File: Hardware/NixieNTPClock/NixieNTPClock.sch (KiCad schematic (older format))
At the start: 54 parts, among them J1 Conn_01x02_Male, Q1 BC850, Q2 Q_NMOS_GDS, Q3 FQT4N25TF, Q4 FQT4N25TF, Q5 FQT4N25TF, Q6 FQT4N25TF, U1 74HC7014, U10 DS18B20, U11 ESP32-nodeMCU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

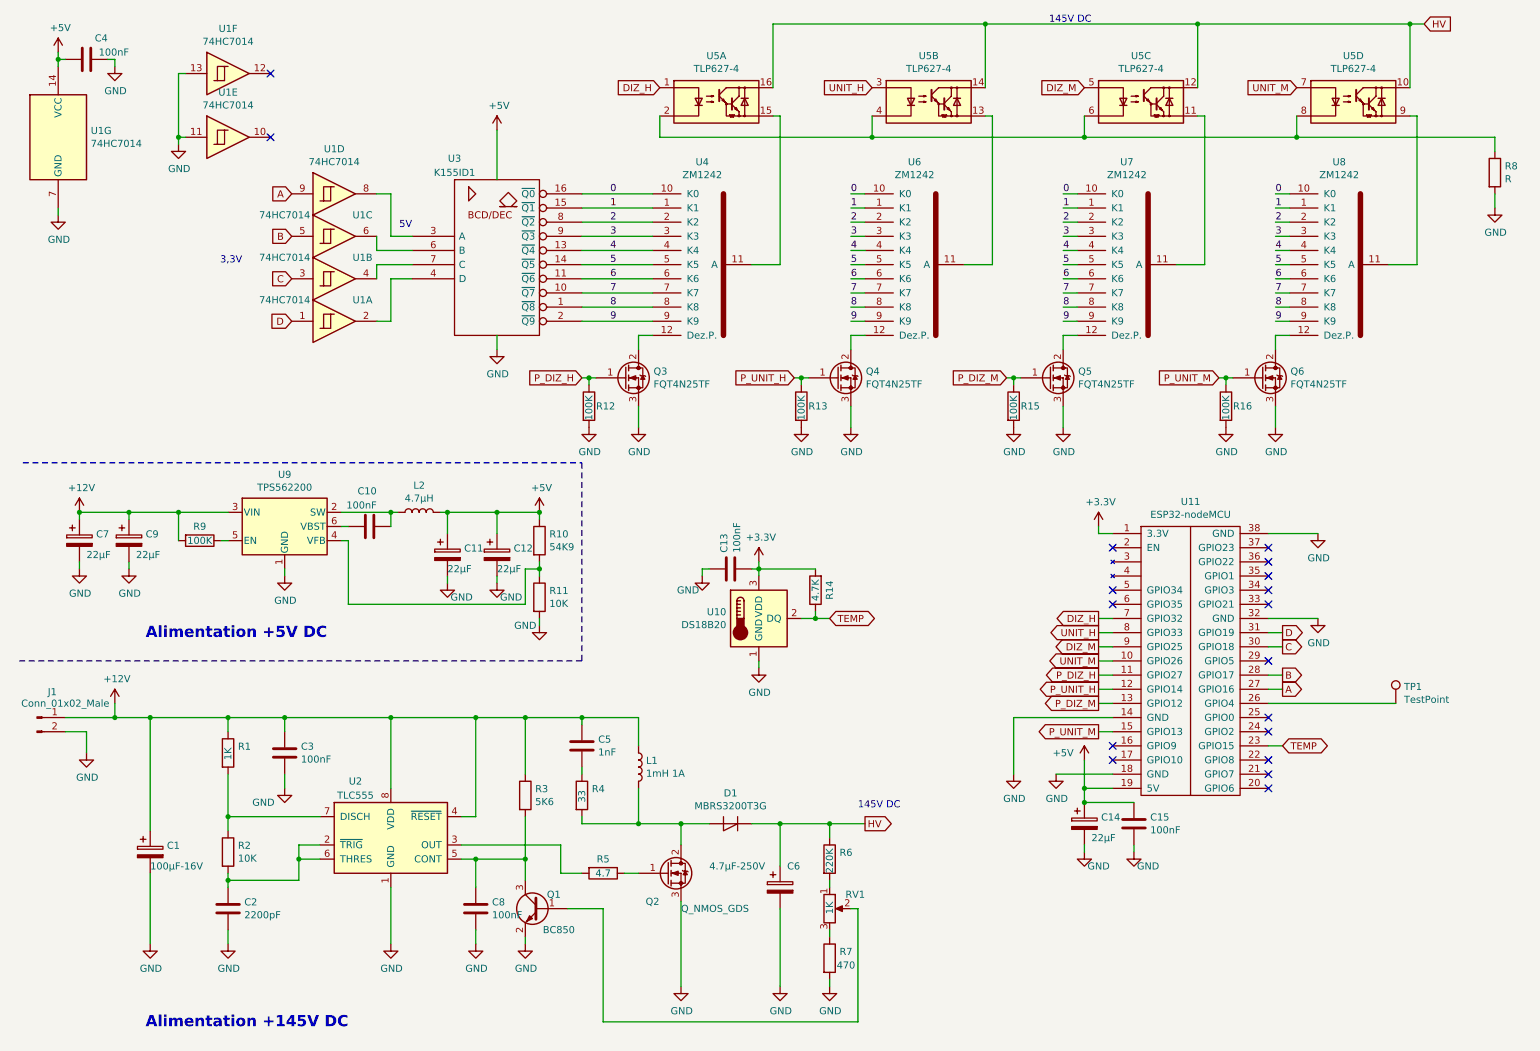
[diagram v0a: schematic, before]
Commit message: Update Schema Add footprint library Finish netlist Started rooting
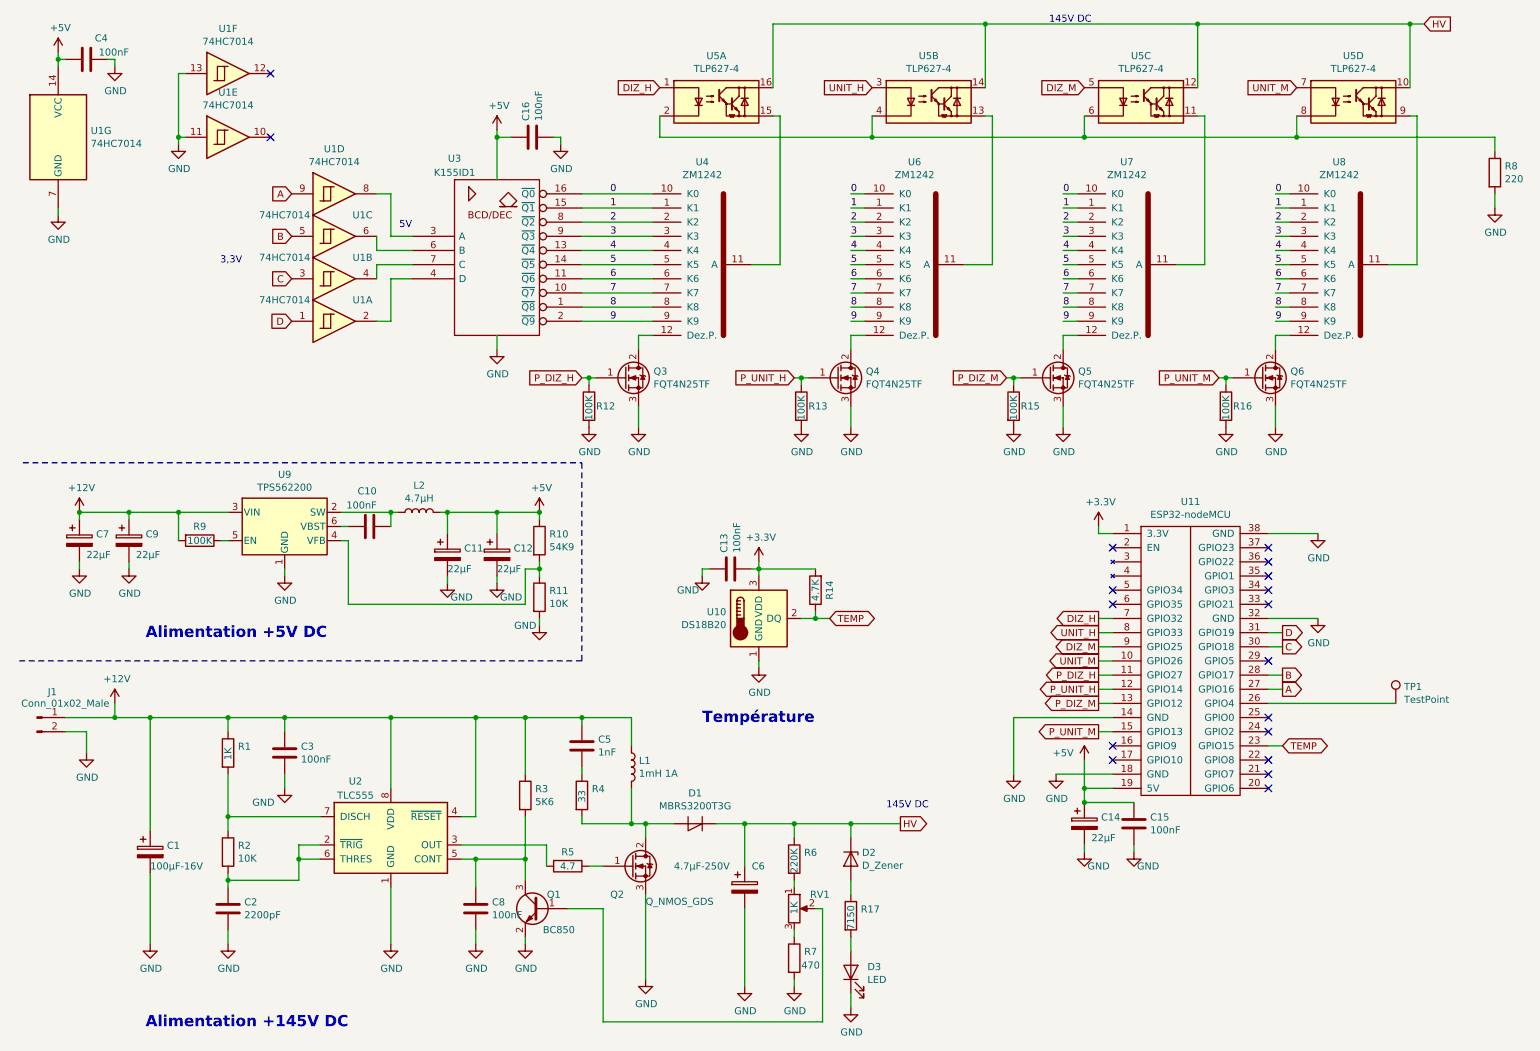
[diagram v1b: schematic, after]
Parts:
- added C16: 100nF, Capacitors_SMD:C_0805_HandSoldering, symbol Device:C
- added D2: D_Zener, Diodes_SMD:D_SMB_Handsoldering, symbol Device:D_Zener
- added D3: LED, Diodes_SMD:D_0603, symbol Device:LED
- added R17: 7150, Resistors_SMD:R_1206_HandSoldering, symbol Device:R
- L2: footprint (none) -> Inductors:SELF-WE-TPC_M; Farnell (none) -> 2066938
- Q1: footprint Package_TO_SOT_SMD:SOT-23 -> TO_SOT_Packages_SMD:SOT-23W_Handsoldering
- R8: value R -> 220
- TP1: footprint (none) -> NixieNTPClock:touch
- U1: footprint Package_SO:SOIC-14_3.9x8.7mm_P1.27mm -> Housings_SOIC:SOIC-14_3.9x8.7mm_Pitch1.27mm
- U10: footprint Package_TO_SOT_THT:TO-92_Inline -> TO_SOT_Packages_THT:TO-92_Inline_Wide
- U11: footprint (none) -> NixieNTPClock:ESP32 NodeMCU AZ
- U4, U6, U7, U8: footprint (none) -> NixieNTPClock:ZM1242
- U5: footprint Package_DIP:DIP-16_W7.62mm -> Housings_DIP:DIP-16_W7.62mm_Socket_LongPads
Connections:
- net +5V: now also C16.1
- net GND: now also C16.2, D3.1 (K)
- net HV: now also D2.1 (K)
- new net: D2.2 (A), R17.1
- new net: D3.2 (A), R17.2
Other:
- note added: "Température"
- moved on the sheet: C6, D1, L1, Q2, R5, R6, R7, RV1
